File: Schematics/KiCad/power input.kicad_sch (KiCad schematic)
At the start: 14 parts, among them J6 B16B-PHDSS(LF)(SN), Q1 IRFZ44NLPBF, U6 TIM 3.5-0911SM, U7 TCAN330GDCNR, U9 ISO7842FDWW

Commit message: Fix all errors and warnings
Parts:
- removed C1, C23, C24, C27: 1210ZC106KAT2A, FP-1210-L_3_3_0_4-W_2_5_0-IPC_A, symbol Altium Content Vault:Power_0_b4654b650e69147ec39a6b967a45e02_Altium Content Vau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
- removed F1: 1206L075/16WR, FP-1206L-MFG, symbol Altium Content Vault:Power_0_5bcf9b9f640e542cf0359d10258e979_Altium Content Vau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
- removed J6: B16B-PHDSS(LF)(SN), FP-B16B-PHDSS_LF_SN-MFG, symbol Altium Content Vault:Power_0_4b6d22b45e2f925f038cba5d936fbcc_Altium Content Vau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
- removed Q1: IRFZ44NLPBF, FP-PG-TO262-3-MFG, symbol Altium Content Vault:Power_0_b09f7f152735e370c1ea22a33fa83d6_Altium Content Vau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
- removed R124: RN73C1J10KB, FP-RN731J-MFG, symbol Altium Content Vault:Power_1_1029c3af85768c4190bb7ad29bc67b5_Altium Content Vau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
- removed R125: 200R 5% 2512(6432), RESC2512(6432)_M, symbol Altium Content Vault:Power_0_RES_Altium Content Vault_0
- removed R126: CRGCQ2512F10K, FP-CRGCQ2512-IPC_C, symbol Altium Content Vault:Power_1_1029c3af85768c4190bb7ad29bc67b5_Altium Content Vau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
- removed U7: TCAN330GDCNR, FP-DCN0008A-MFG, symbol Altium Content Vault:Power_0_22681b49c22ad38c6a4e12e04c36c7a_Altium Content Vau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
- removed U9: ISO7842FDWW, FP-DWW0016A-MFG, symbol Altium Content Vault:Power_0_438c63db371af18872a5eb11a908997_Altium Content Vau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
- added 9: ~, symbol TempSenseSymbols:ISO7842FDWW
- added C1, C10, C11, C8, C9: 10u, Capacitor_SMD:C_0603_1608Metric, symbol Device:C
- added F2: 750mA, symbol Device:Fuse
- added J7: Conn_02x08_Odd_Even, symbol Connector_Generic:Conn_02x08_Odd_Even
- added Q2: 2N7002H, Package_TO_SOT_SMD:SOT-23, symbol Transistor_FET:2N7002H
- added R61, R65: 10k, Resistor_SMD:R_0603_1608Metric, symbol Device:R_US
- added U10: TCAN330G, symbol Interface_CAN_LIN:TCAN330G
- added U12: LD1117S33TR_SOT223, Package_TO_SOT_SMD:SOT-223-3_TabPin2, symbol Regulator_Linear:LD1117S33TR_SOT223
- 6: renamed from U6; value TIM 3.5-0911SM -> ~
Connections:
- net +5V: now also 9.10 (EN2), C8.1, U12.3 (VI)
- net Fault Line 1: now also 9.11 (IND)
- net GND: now also 9.15 (GND2), 9.9 (GND2), C11.2, C8.2, U12.1 (GND)
- net GNDPWR: now also 9.2 (GND1), 9.8 (GND1), C1.2, C10.2, C9.2, J7.13 (Pin_13), Q2.2 (S), R61.2, U10.2 (GND), U10.8 (S)
- net RXD: now also 9.13 (OUTB)
- net TXD: now also 9.12 (INC)
- net +3.3VP: now reaches PS1.3 (OUT)
- net +3.3VP: now also 9.1 (VCC1), C10.1, R65.1, U10.3 (VCC), U10.5 (SHDN)
- net +12V: now reaches 6.16 (+VIN), PS1.1 (IN)
- net +12V: now also C1.1, C9.1, F2.1
- new net: 9.7 (EN1), R65.2
- new net: 9.5 (OUTC), U10.1 (TXD)
- new net: 9.4 (INB), U10.4 (RXD)
- new net: J7.9 (Pin_9), U10.6 (CANL)
- new net: J7.7 (Pin_7), U10.7 (CANH)
- new net: F2.2, J7.1 (Pin_1)
- new net: J7.3 (Pin_3), Q2.3 (D)
- new net: 9.6 (OUTD), Q2.1 (G), R61.1
- new net +3V3: C11.1, U12.2 (VO)
- no-connect marks 6 -> 15
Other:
- note added: "GLV Side"
- note added: "HV Side"
- note removed: "Lv_gnd"
- moved on the sheet: 6, PS1

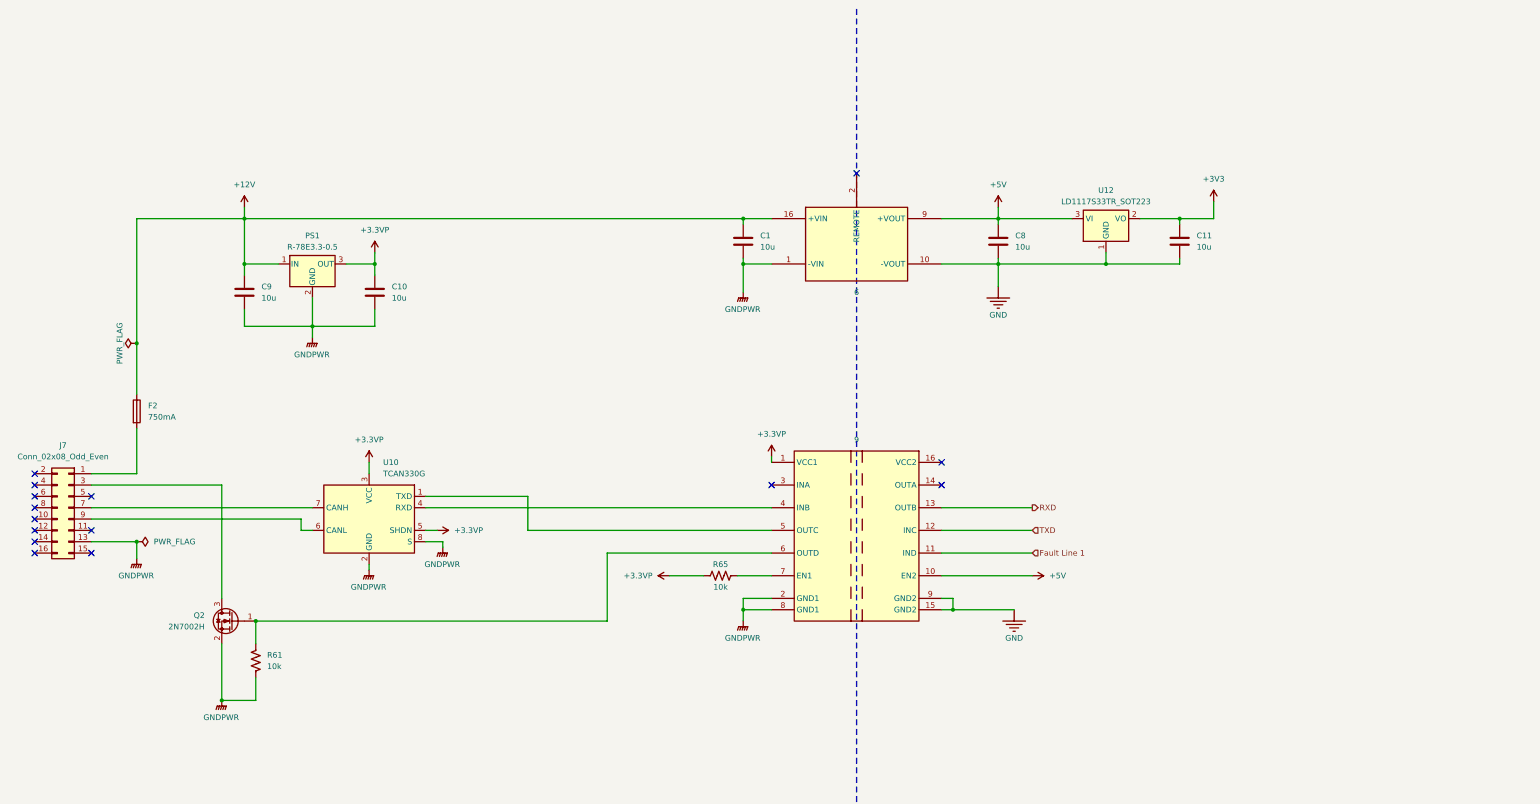
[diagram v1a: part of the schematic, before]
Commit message: Condense layout to 2 layers
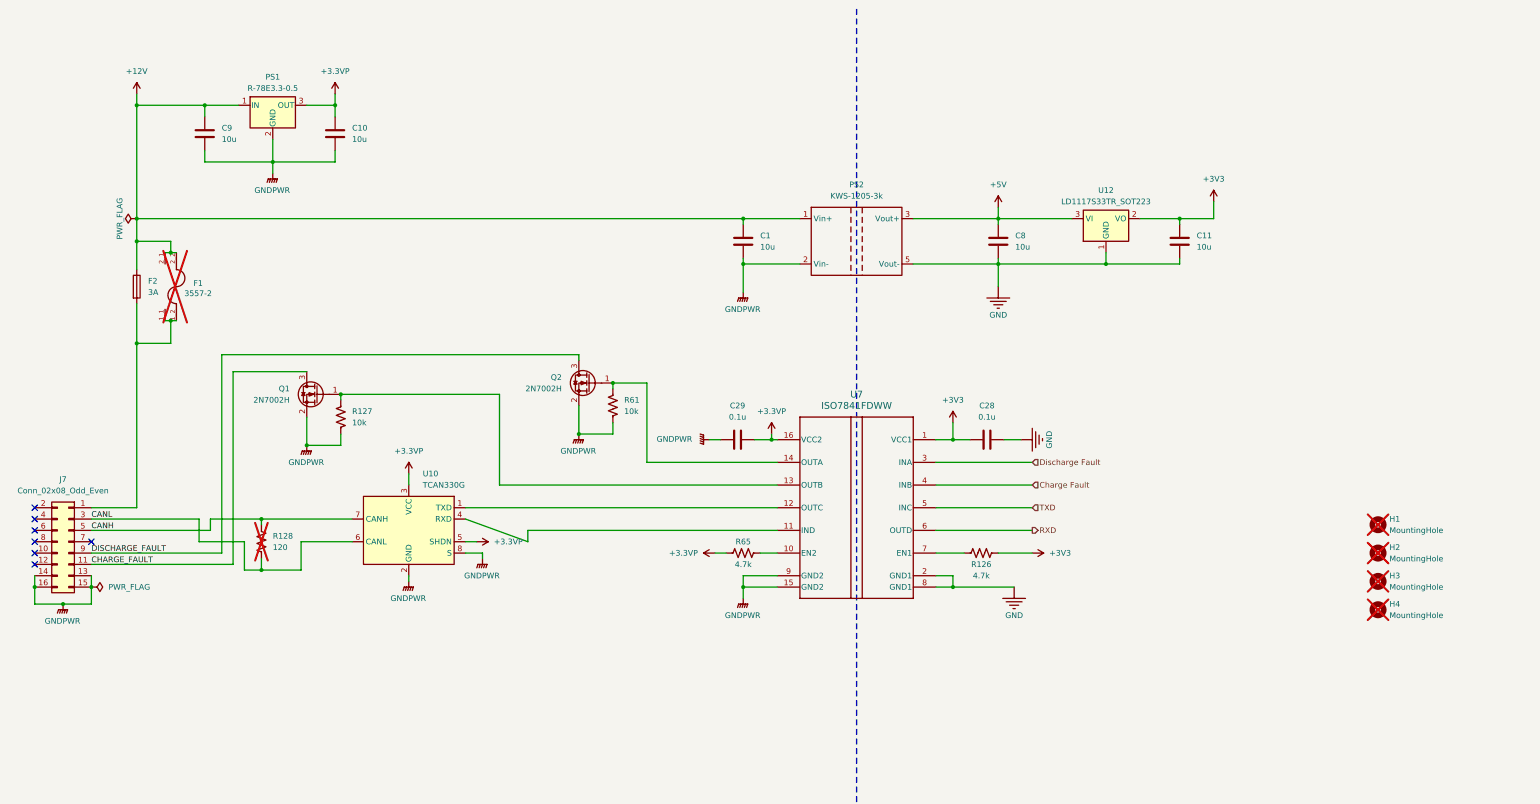
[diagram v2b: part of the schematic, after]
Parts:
- removed 6: ~, symbol TempSenseSymbols:TIM_3.5-0911SM
- removed 9: ~, symbol TempSenseSymbols:ISO7842FDWW
- added C28, C29: 0.1u, Capacitor_SMD:C_0603_1608Metric, symbol Device:C
- added F1: 3557-2, Personal:FUSE_3557-2, symbol Personal_Relays:3557-2
- added H1, H2, H3, H4: MountingHole, MountingHole:MountingHole_6.4mm_M6, symbol Mechanical:MountingHole
- added PS2: KWS-1205-3k, TempSenseFootprints:KWS-1205-3K, symbol TempSenseSymbols:KWS-1205-3K
- added Q1: 2N7002H, Package_TO_SOT_SMD:SOT-23, symbol Transistor_FET:2N7002H
- added R126: 4.7k, Resistor_SMD:R_0603_1608Metric, symbol Device:R_US
- added R127: 10k, Resistor_SMD:R_0603_1608Metric, symbol Device:R_US
- added R128: 120, Resistor_SMD:R_0603_1608Metric, symbol Device:R_US
- added U7: ISO7841FDWW, TempSenseFootprints:DWW0016A_N, symbol TempSenseSymbols:ISO7841FDWW
- F2: value 750mA -> 3A; footprint (none) -> Fuse:Fuse_0603_1608Metric; MPN (none) -> SF-0603S300-2
- J7: footprint (none) -> Connector_PinSocket_2.00mm:PinSocket_2x08_P2.00mm_Vertical; MPN (none) -> B16B-PHDSS
- R65: value 10k -> 4.7k
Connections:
- net +12V: now also F1.2_1, F1.2_2, PS2.1 (Vin+)
- net +3.3VP: now also C29.1, U7.16 (VCC2)
- net +3V3: now also C28.1, R126.2, U7.1 (VCC1)
- net +5V: now also PS2.3 (Vout+)
- net GND: now also C28.2, PS2.5 (Vout-), U7.2 (GND1), U7.8 (GND1)
- net GNDPWR: now also J7.14 (Pin_14), J7.15 (Pin_15), J7.16 (Pin_16), C29.2, PS2.2 (Vin-), Q1.2 (S), R127.2, U7.15 (GND2), U7.9 (GND2)
- net RXD: now also U7.6 (OUTD)
- net TXD: now also U7.5 (INC)
- net at R65.2: now also U7.10 (EN2)
- net at U10.1 (TXD): now also U7.12 (OUTC)
- net at U10.4 (RXD): now also U7.11 (IND)
- net CANL: now reaches U10.6 (CANL)
- net CANL: now also J7.3 (Pin_3), R128.2; no longer J7.9 (Pin_9)
- net at J7.7 (Pin_7): no longer U10.7 (CANH)
- net at F2.2, J7.1 (Pin_1): now also F1.1_1, F1.1_2
- net CHARGE_FAULT: now reaches J7.11 (Pin_11)
- net CHARGE_FAULT: now also Q1.3 (D)
- net DISCHARGE_FAULT: now reaches Q2.3 (D)
- net DISCHARGE_FAULT: now also J7.9 (Pin_9); no longer J7.3 (Pin_3)
- net CANH: now reaches J7.5 (Pin_5)
- net CANH: now also U10.7 (CANH), R128.1
- net at Q2.1 (G), R61.1: now also U7.14 (OUTA)
- new net: R126.1, U7.7 (EN1)
- new net: Q1.1 (G), R127.1, U7.13 (OUTB)
- new net Charge Fault: U7.4 (INB)
- new net Discharge Fault: U7.3 (INA)
- no-connect marks 15 -> 7
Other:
- moved on the sheet: C10, C9, F2, J7, PS1, Q2, R61, R65, U10
